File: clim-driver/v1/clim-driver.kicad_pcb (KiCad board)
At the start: 2 copper layers, 95 x 50 mm, 32 parts, among them J1 Conn_01x03_Male, J2 Screw_Terminal_01x02, J3 Screw_Terminal_01x02, J4 Conn_01x07_Pin, U1 R-785.0-1.0, U2 WeMos_D1_mini, U3 4N35, U4 4N35, U5 4N35, U6 4N35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

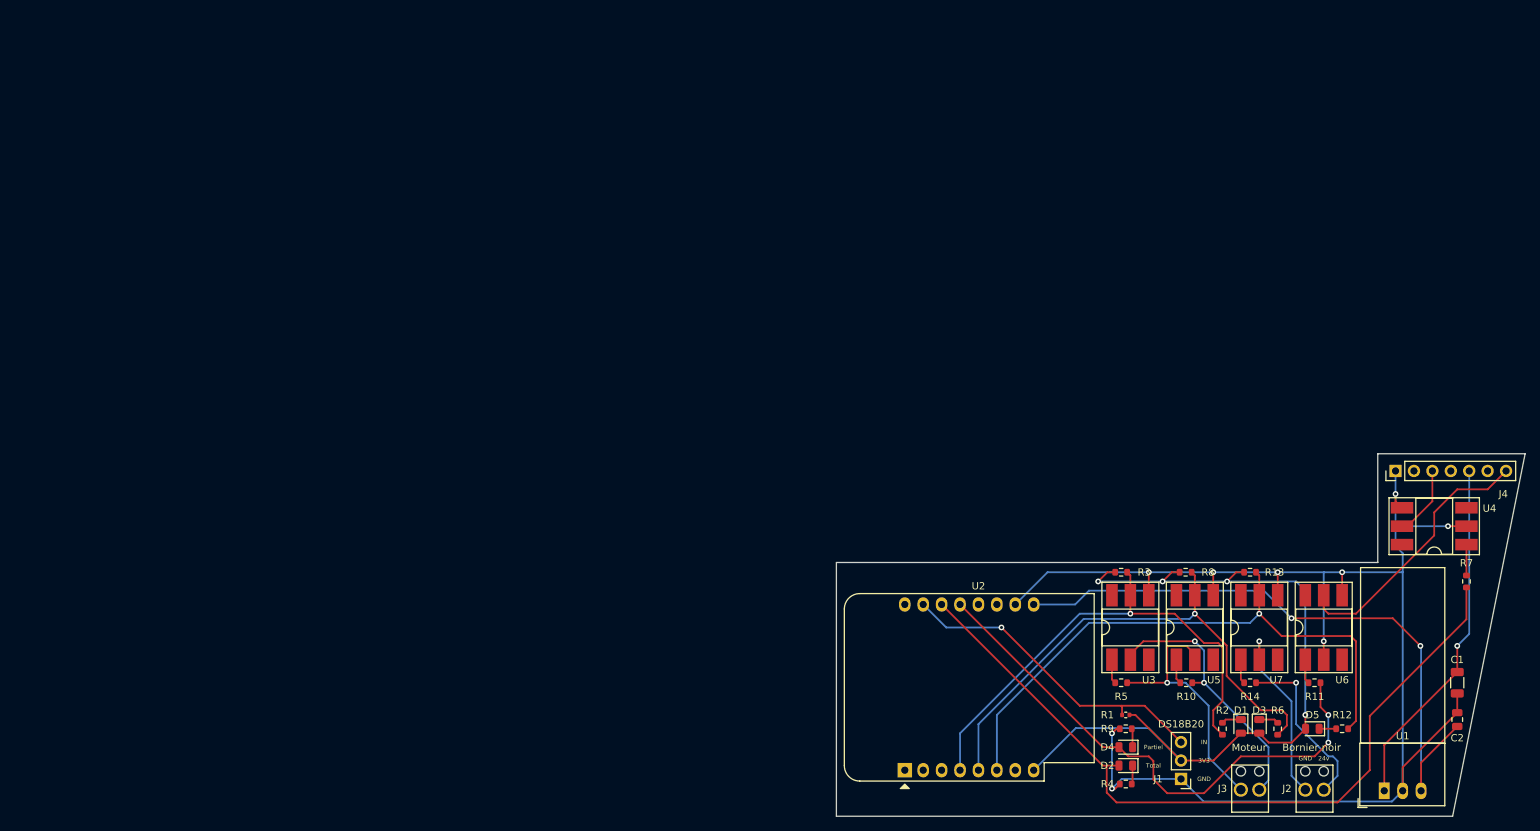
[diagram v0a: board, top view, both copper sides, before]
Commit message: update schematic
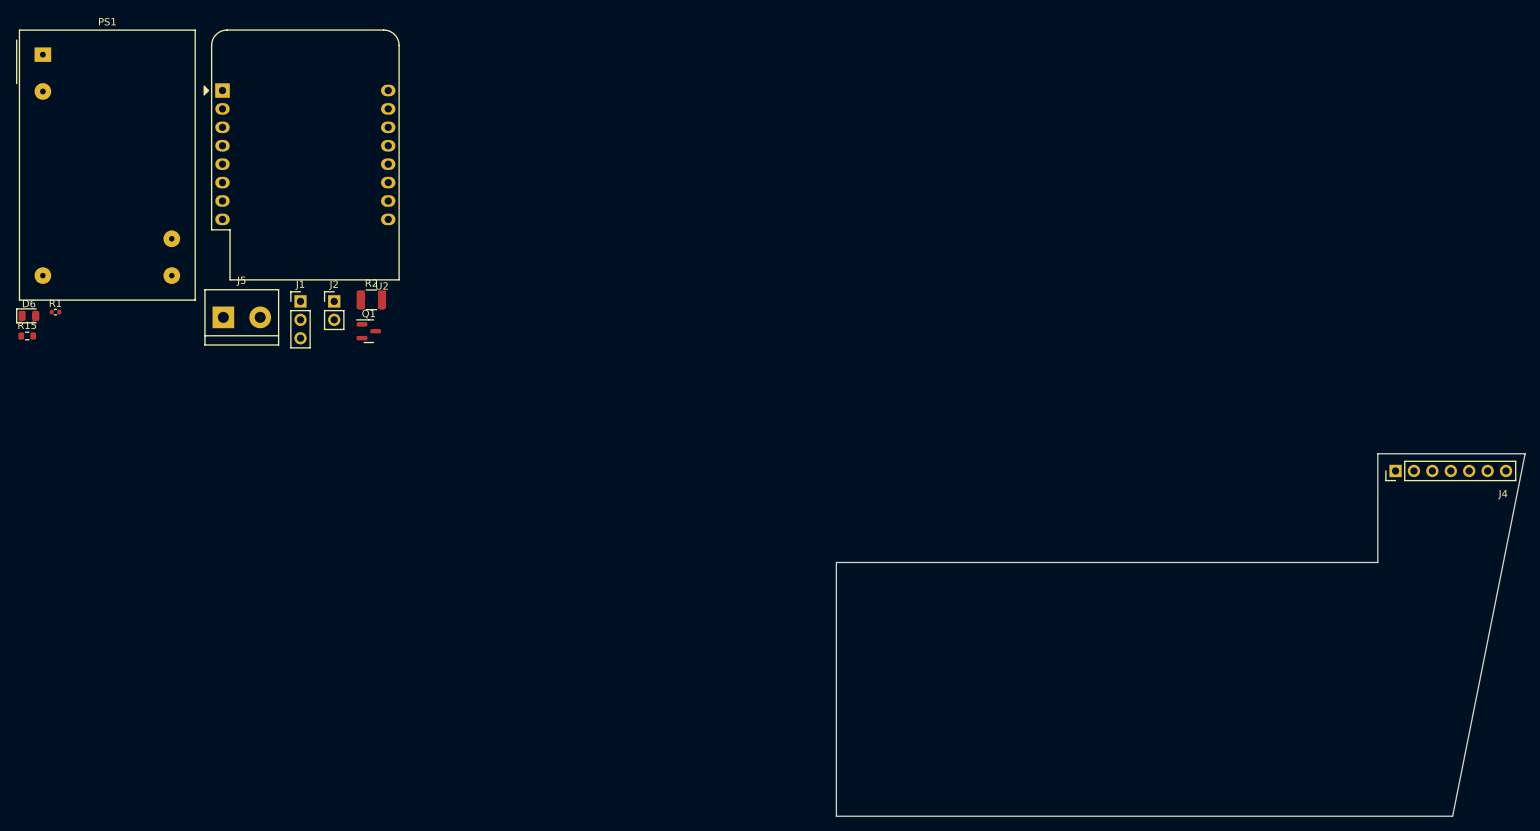
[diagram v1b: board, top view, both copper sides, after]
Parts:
- removed C1: 10μF/50V, Capacitor_SMD:C_1206_3216Metric
- removed C2: 22μF/10V, Capacitor_SMD:C_0805_2012Metric
- removed D1, D2, D3, D4, D5: LED, Diode_SMD:D_0805_2012Metric
- removed J3: Screw_Terminal_01x02, mylife-footprints:RS PRO Terminal Small x2
- removed R10, R14, R5: 2.2KΩ, Resistor_SMD:R_0603_1608Metric
- removed R11, R7: 220Ω, Resistor_SMD:R_0603_1608Metric
- removed R12, R4, R6, R9: 1KΩ, Resistor_SMD:R_0603_1608Metric
- removed R13, R3, R8: 10KΩ, Resistor_SMD:R_0603_1608Metric
- removed U1: R-785.0-1.0, Converter_DCDC:Converter_DCDC_RECOM_R-78E-0.5_THT
- removed U3, U4, U5, U6, U7: 4N35, Package_DIP:DIP-6_W8.89mm_SMDSocket_LongPads
- added D6: LED, Diode_SMD:D_0805_2012Metric, F.Cu at (1.75, 39.6)
- added J5: Screw_Terminal_01x02, TerminalBlock:TerminalBlock_bornier-2_P5.08mm, F.Cu at (28.6, 39.8)
- added PS1: Alim RS PRO 5V 1A, Converter_ACDC:Converter_ACDC_MeanWell_IRM-03-xx_THT, F.Cu at (3.67, 3.54)
- added Q1: BSS138, Package_TO_SOT_SMD:SOT-23, F.Cu at (48.6, 41.7)
- added R15: 1KΩ, Resistor_SMD:R_0603_1608Metric, F.Cu at (1.50, 42.3)
- J2: value Screw_Terminal_01x02 -> Conn_01x02_Pin; footprint mylife-footprints:RS PRO Terminal Small x2 -> Connector_PinHeader_2.54mm:PinHeader_1x02_P2.54mm_Vertical
- R2: value 1KΩ -> 18Ω/0.5W; footprint Resistor_SMD:R_0603_1608Metric -> Resistor_SMD:R_1210_3225Metric
- moved R1 157.7 mm to (5.41, 39.0), turned to 0 degrees
- moved J2 152.2 mm to (43.9, 37.6), turned to 0 degrees
- moved J1 138.2 mm to (39.2, 37.6), turned to 0 degrees
- moved U2 132.8 mm to (28.4, 8.48), turned to 0 degrees
- moved R2 131.5 mm to (49.0, 37.4), turned to 0 degrees
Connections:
- J2 pad 1: Net-(J2-Pin_1) -> +3V3
- R2 pad 1: Net-(U2-SCK/D5) -> Net-(Q1-D)
- R2 pad 2: Net-(D1-K) -> Net-(J2-Pin_2)
- U2 pad 13: Net-(D4-A) -> unconnected-(U2-SDA/D2-Pad13)
- U2 pad 4: Net-(U2-SCK/D5) -> unconnected-(U2-SCK/D5-Pad4)
- U2 pad 5: Net-(U2-MISO/D6) -> unconnected-(U2-MISO/D6-Pad5)
- U2 pad 6: Net-(U2-MOSI/D7) -> unconnected-(U2-MOSI/D7-Pad6)
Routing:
- net GND: track 206.0 -> 0.00 mm, vias 9 -> 0
- net +3V3: track 111.2 -> 0.00 mm, vias 4 -> 0
- net Net-(Q1-G): track 106.8 -> 0.00 mm
- net +5V: track 88.3 -> 0.00 mm, vias 2 -> 0
- net Net-(U2-MOSI/D7): track 82.9 -> 0.00 mm, vias 1 -> 0
- net Net-(D4-A): track 74.7 -> 0.00 mm, vias 2 -> 0
- net Net-(U2-MISO/D6): track 72.6 -> 0.00 mm, vias 1 -> 0
- net Net-(U2-SCK/D5): track 69.1 -> 0.00 mm, vias 1 -> 0
- net +24V: track 49.0 -> 0.00 mm, vias 1 -> 0
- net Net-(J1-Pin_3): track 44.7 -> 0.00 mm, vias 1 -> 0
- net Net-(J4-Pin_7): track 37.3 -> 0.00 mm
- net Net-(J3-Pin_1): track 37.2 -> 0.00 mm, vias 2 -> 0
- net Net-(J3-Pin_2): track 36.0 -> 0.00 mm, vias 1 -> 0
- net Net-(J2-Pin_2): track 25.6 -> 0.00 mm, vias 1 -> 0
- net Net-(J2-Pin_1): track 23.8 -> 0.00 mm, vias 1 -> 0
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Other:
- board text removed: "24v"
- board text removed: "3V3"
- board text removed: "Bornier noir"
- board text removed: "DS18B20"
- board text removed: "GND"
- board text removed: "IN"
- board text removed: "Moteur"
- board text removed: "Partiel"
- board text removed: "Total"

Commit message: add pcb size
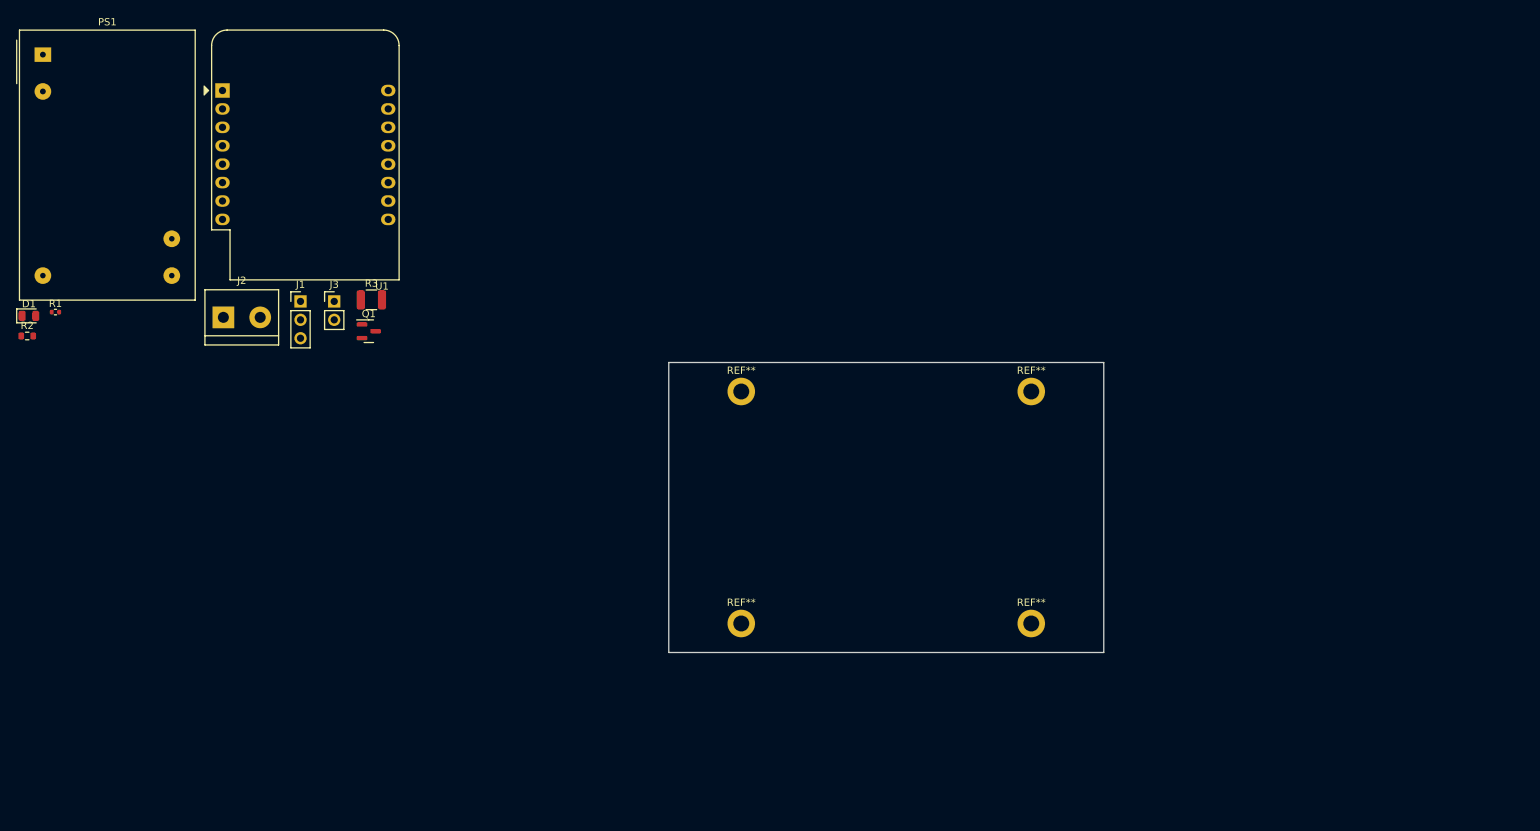
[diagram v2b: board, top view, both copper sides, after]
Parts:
- removed J4: Conn_01x07_Pin, Connector_PinHeader_2.54mm:PinHeader_1x07_P2.54mm_Vertical
- added REF**: MountingHole_2.2mm_M2_DIN965_Pad, MountingHole:MountingHole_2.2mm_M2_DIN965_Pad, F.Cu at (100.0, 82.0)
- added REF**: MountingHole_2.2mm_M2_DIN965_Pad, MountingHole:MountingHole_2.2mm_M2_DIN965_Pad, F.Cu at (100.0, 50.0)
- added REF**: MountingHole_2.2mm_M2_DIN965_Pad, MountingHole:MountingHole_2.2mm_M2_DIN965_Pad, F.Cu at (140.0, 50.0)
- added REF**: MountingHole_2.2mm_M2_DIN965_Pad, MountingHole:MountingHole_2.2mm_M2_DIN965_Pad, F.Cu at (140.0, 82.0)
- renumbered D6 to D1, J5 to J2, J2 to J3, R15 to R2, R2 to R3, U2 to U1
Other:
- board size 95 x 50 mm -> 60 x 40 mm

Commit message: wip pcb
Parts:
- moved PS1 133.9 mm to (128.9, 50.8)
- moved U1 110.3 mm to (114.5, 77.5), turned to 180 degrees
- moved J2 93.9 mm to (121.3, 54.6), turned to 90 degrees
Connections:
- J2 pad 1: LINE -> NEUT
- J2 pad 2: NEUT -> LINE
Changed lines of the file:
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@@
   )
   (footprint "TerminalBlock:TerminalBlock_bornier-2_P5.08mm" (layer "F.Cu")
-    (at 28.565 39.775)
+    (at 121.285 54.61 90)
     (descr "simple 2-pin terminal block, pitch 5.08mm, revamped version of bornier2")
     (tags "terminal block bornier2")
@@
     (property "ki_keywords" "screw terminal")
     (attr through_hole)
-    (fp_text reference "J2" (at 2.54 -5.08) (layer "F.SilkS")
-        (effects (font (size 1 1) (thickness 0.15)))
-    )
-    (fp_text value "Screw_Terminal_01x02" (at 2.54 5.08) (layer "F.Fab")
-        (effects (font (size 1 1) (thickness 0.15)))
-    )
-    (fp_text user "${REFERENCE}" (at 2.54 0) (layer "F.Fab")
+    (fp_text reference "J2" (at 2.54 -5.08 90) (layer "F.SilkS")
+        (effects (font (size 1 1) (thickness 0.15)))
+    )
+    (fp_text value "Screw_Terminal_01x02" (at 2.54 5.08 90) (layer "F.Fab")
+        (effects (font (size 1 1) (thickness 0.15)))
+    )
+    (fp_text user "${REFERENCE}" (at 2.54 0 90) (layer "F.Fab")
         (effects (font (size 1 1) (thickness 0.15)))
     )
@@
     (fp_line (start 7.54 3.75) (end 7.54 -3.75)
       (stroke (width 0.1) (type solid)) (layer "F.Fab"))
-    (pad "1" thru_hole rect (at 0 0) (size 3 3) (drill 1.52) (layers "*.Cu" "*.Mask")
-      (net 4 "LINE") (pinfunction "Pin_1") (pintype "passive"))
-    (pad "2" thru_hole circle (at 5.08 0) (size 3 3) (drill 1.52) (layers "*.Cu" "*.Mask")
-      (net 5 "NEUT") (pinfunction "Pin_2") (pintype "passive"))
+    (pad "1" thru_hole rect (at 0 0 90) (size 3 3) (drill 1.52) (layers "*.Cu" "*.Mask")
+      (net 5 "NEUT") (pinfunction "Pin_1") (pintype "passive"))
+    (pad "2" thru_hole circle (at 5.08 0 90) (size 3 3) (drill 1.52) (layers "*.Cu" "*.Mask")
+      (net 4 "LINE") (pinfunction "Pin_2") (pintype "passive"))
     (model "${KICAD6_3DMODEL_DIR}/TerminalBlock.3dshapes/TerminalBlock_bornier-2_P5.08mm.wrl"
       (offset (xyz 2.539999962 0 0))
@@
   )
   (footprint "Module:WEMOS_D1_mini_light" (layer "F.Cu")
-    (at 28.445 8.485)
+    (at 114.45 77.47 180)
     (descr "16-pin module, column spacing 22.86 mm (900 mils), https://wiki.wemos.cc/products:d1:d1_mini, https://c1.staticflickr.com/1/734/31400410271_f278b087db_z.jpg")
     (tags "ESP8266 WiFi microcontroller")
@@
     (fp_arc (start 22.25 -8.21) (mid 23.658356 -7.610071) (end 24.23 -6.19)
       (stroke (width 0.1) (type solid)) (layer "F.Fab"))
-    (pad "1" thru_hole rect (at 0 0) (size 2 2) (drill 1) (layers "*.Cu" "*.Mask")
+    (pad "1" thru_hole rect (at 0 0 180) (size 2 2) (drill 1) (layers "*.Cu" "*.Mask")
       (net 22 "unconnected-(U1-~{RST}-Pad1)") (pinfunction "~{RST}") (pintype "input"))
-    (pad "2" thru_hole oval (at 0 2.54) (size 2 1.6) (drill 1) (layers "*.Cu" "*.Mask")
+    (pad "2" thru_hole oval (at 0 2.54 180) (size 2 1.6) (drill 1) (layers "*.Cu" "*.Mask")
       (net 21 "unconnected-(U1-A0-Pad2)") (pinfunction "A0") (pintype "input"))
-    (pad "3" thru_hole oval (at 0 5.08) (size 2 1.6) (drill 1) (layers "*.Cu" "*.Mask")
+    (pad "3" thru_hole oval (at 0 5.08 180) (size 2 1.6) (drill 1) (layers "*.Cu" "*.Mask")
       (net 20 "unconnected-(U1-D0-Pad3)") (pinfunction "D0") (pintype "bidirectional"))
-    (pad "4" thru_hole oval (at 0 7.62) (size 2 1.6) (drill 1) (layers "*.Cu" "*.Mask")
+    (pad "4" thru_hole oval (at 0 7.62 180) (size 2 1.6) (drill 1) (layers "*.Cu" "*.Mask")
       (net 19 "unconnected-(U1-SCK{slash}D5-Pad4)") (pinfunction "SCK/D5") (pintype "bidirectional"))
-    (pad "5" thru_hole oval (at 0 10.16) (size 2 1.6) (drill 1) (layers "*.Cu" "*.Mask")
+    (pad "5" thru_hole oval (at 0 10.16 180) (size 2 1.6) (drill 1) (layers "*.Cu" "*.Mask")
       (net 18 "unconnected-(U1-MISO{slash}D6-Pad5)") (pinfunction "MISO/D6") (pintype "bidirectional"))
-    (pad "6" thru_hole oval (at 0 12.7) (size 2 1.6) (drill 1) (layers "*.Cu" "*.Mask")
+    (pad "6" thru_hole oval (at 0 12.7 180) (size 2 1.6) (drill 1) (layers "*.Cu" "*.Mask")
       (net 17 "unconnected-(U1-MOSI{slash}D7-Pad6)") (pinfunction "MOSI/D7") (pintype "bidirectional"))
-    (pad "7" thru_hole oval (at 0 15.24) (size 2 1.6) (drill 1) (layers "*.Cu" "*.Mask")
+    (pad "7" thru_hole oval (at 0 15.24 180) (size 2 1.6) (drill 1) (layers "*.Cu" "*.Mask")
       (net 16 "unconnected-(U1-CS{slash}D8-Pad7)") (pinfunction "CS/D8") (pintype "bidirectional"))
-    (pad "8" thru_hole oval (at 0 17.78) (size 2 1.6) (drill 1) (layers "*.Cu" "*.Mask")
+    (pad "8" thru_hole oval (at 0 17.78 180) (size 2 1.6) (drill 1) (layers "*.Cu" "*.Mask")
       (net 3 "+3V3") (pinfunction "3V3") (pintype "power_out"))
-    (pad "9" thru_hole oval (at 22.86 17.78) (size 2 1.6) (drill 1) (layers "*.Cu" "*.Mask")
+    (pad "9" thru_hole oval (at 22.86 17.78 180) (size 2 1.6) (drill 1) (layers "*.Cu" "*.Mask")
       (net 2 "+5V") (pinfunction "5V") (pintype "power_in"))
-    (pad "10" thru_hole oval (at 22.86 15.24) (size 2 1.6) (drill 1) (layers "*.Cu" "*.Mask")
+    (pad "10" thru_hole oval (at 22.86 15.24 180) (size 2 1.6) (drill 1) (layers "*.Cu" "*.Mask")
       (net 1 "GND") (pinfunction "GND") (pintype "power_in"))
-    (pad "11" thru_hole oval (at 22.86 12.7) (size 2 1.6) (drill 1) (layers "*.Cu" "*.Mask")
+    (pad "11" thru_hole oval (at 22.86 12.7 180) (size 2 1.6) (drill 1) (layers "*.Cu" "*.Mask")
       (net 15 "unconnected-(U1-D4-Pad11)") (pinfunction "D4") (pintype "bidirectional"))
-    (pad "12" thru_hole oval (at 22.86 10.16) (size 2 1.6) (drill 1) (layers "*.Cu" "*.Mask")
+    (pad "12" thru_hole oval (at 22.86 10.16 180) (size 2 1.6) (drill 1) (layers "*.Cu" "*.Mask")
       (net 14 "unconnected-(U1-D3-Pad12)") (pinfunction "D3") (pintype "bidirectional"))
-    (pad "13" thru_hole oval (at 22.86 7.62) (size 2 1.6) (drill 1) (layers "*.Cu" "*.Mask")
+    (pad "13" thru_hole oval (at 22.86 7.62 180) (size 2 1.6) (drill 1) (layers "*.Cu" "*.Mask")
       (net 13 "unconnected-(U1-SDA{slash}D2-Pad13)") (pinfunction "SDA/D2") (pintype "bidirectional"))
-    (pad "14" thru_hole oval (at 22.86 5.08) (size 2 1.6) (drill 1) (layers "*.Cu" "*.Mask")
+    (pad "14" thru_hole oval (at 22.86 5.08 180) (size 2 1.6) (drill 1) (layers "*.Cu" "*.Mask")
       (net 7 "Net-(Q1-G)") (pinfunction "SCL/D1") (pintype "bidirectional"))
-    (pad "15" thru_hole oval (at 22.86 2.54) (size 2 1.6) (drill 1) (layers "*.Cu" "*.Mask")
+    (pad "15" thru_hole oval (at 22.86 2.54 180) (size 2 1.6) (drill 1) (layers "*.Cu" "*.Mask")
       (net 9 "Net-(J1-Pin_3)") (pinfunction "RX") (pintype "input"))
-    (pad "16" thru_hole oval (at 22.86 0) (size 2 1.6) (drill 1) (layers "*.Cu" "*.Mask")
+    (pad "16" thru_hole oval (at 22.86 0 180) (size 2 1.6) (drill 1) (layers "*.Cu" "*.Mask")
       (net 12 "unconnected-(U1-TX-Pad16)") (pinfunction "TX") (pintype "output"))
     (model "${KICAD6_3DMODEL_DIR}/Module.3dshapes/WEMOS_D1_mini_light.wrl"
@@
   )
   (footprint "Converter_ACDC:Converter_ACDC_MeanWell_IRM-03-xx_THT" (layer "F.Cu")
-    (at 3.67 3.535)
+    (at 128.905 50.8)
     (descr "ACDC-Converter, 3W, Meanwell, IRM-03, THT, https://www.meanwell.com/Upload/PDF/IRM-03/IRM-03-SPEC.PDF")
     (tags "ACDC-Converter 3W THT")
